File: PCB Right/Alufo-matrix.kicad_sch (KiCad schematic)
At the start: 62 parts, among them K11 PG1350, K12 PG1350, K13 PG1350, K14 PG1350, K15 PG1350, K16 PG1350, K21 PG1350, K22 PG1350, K23 PG1350, K24 PG1350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

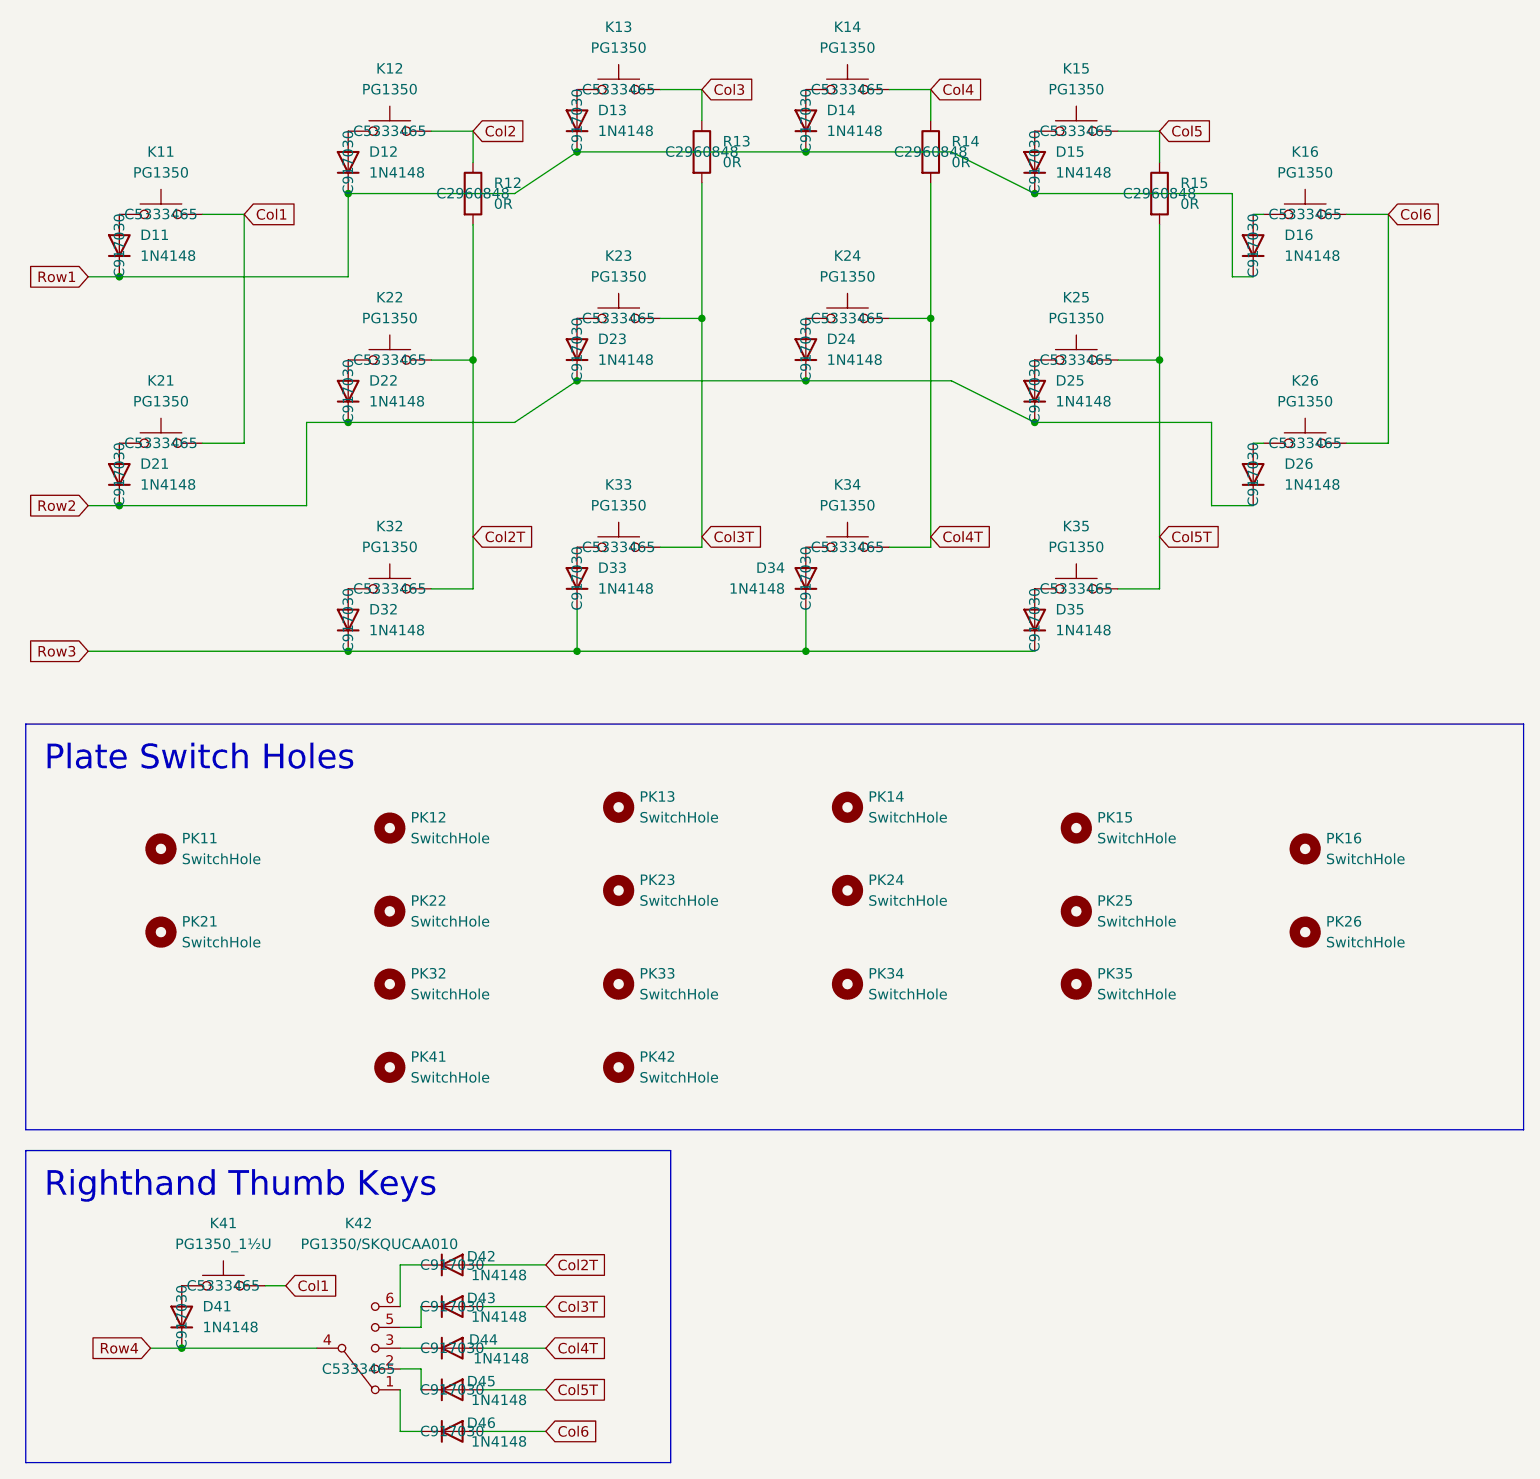
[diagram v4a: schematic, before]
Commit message: Update LCSC part number for USB ports
Also hide LCSC numbers erroneously showing in schematic.
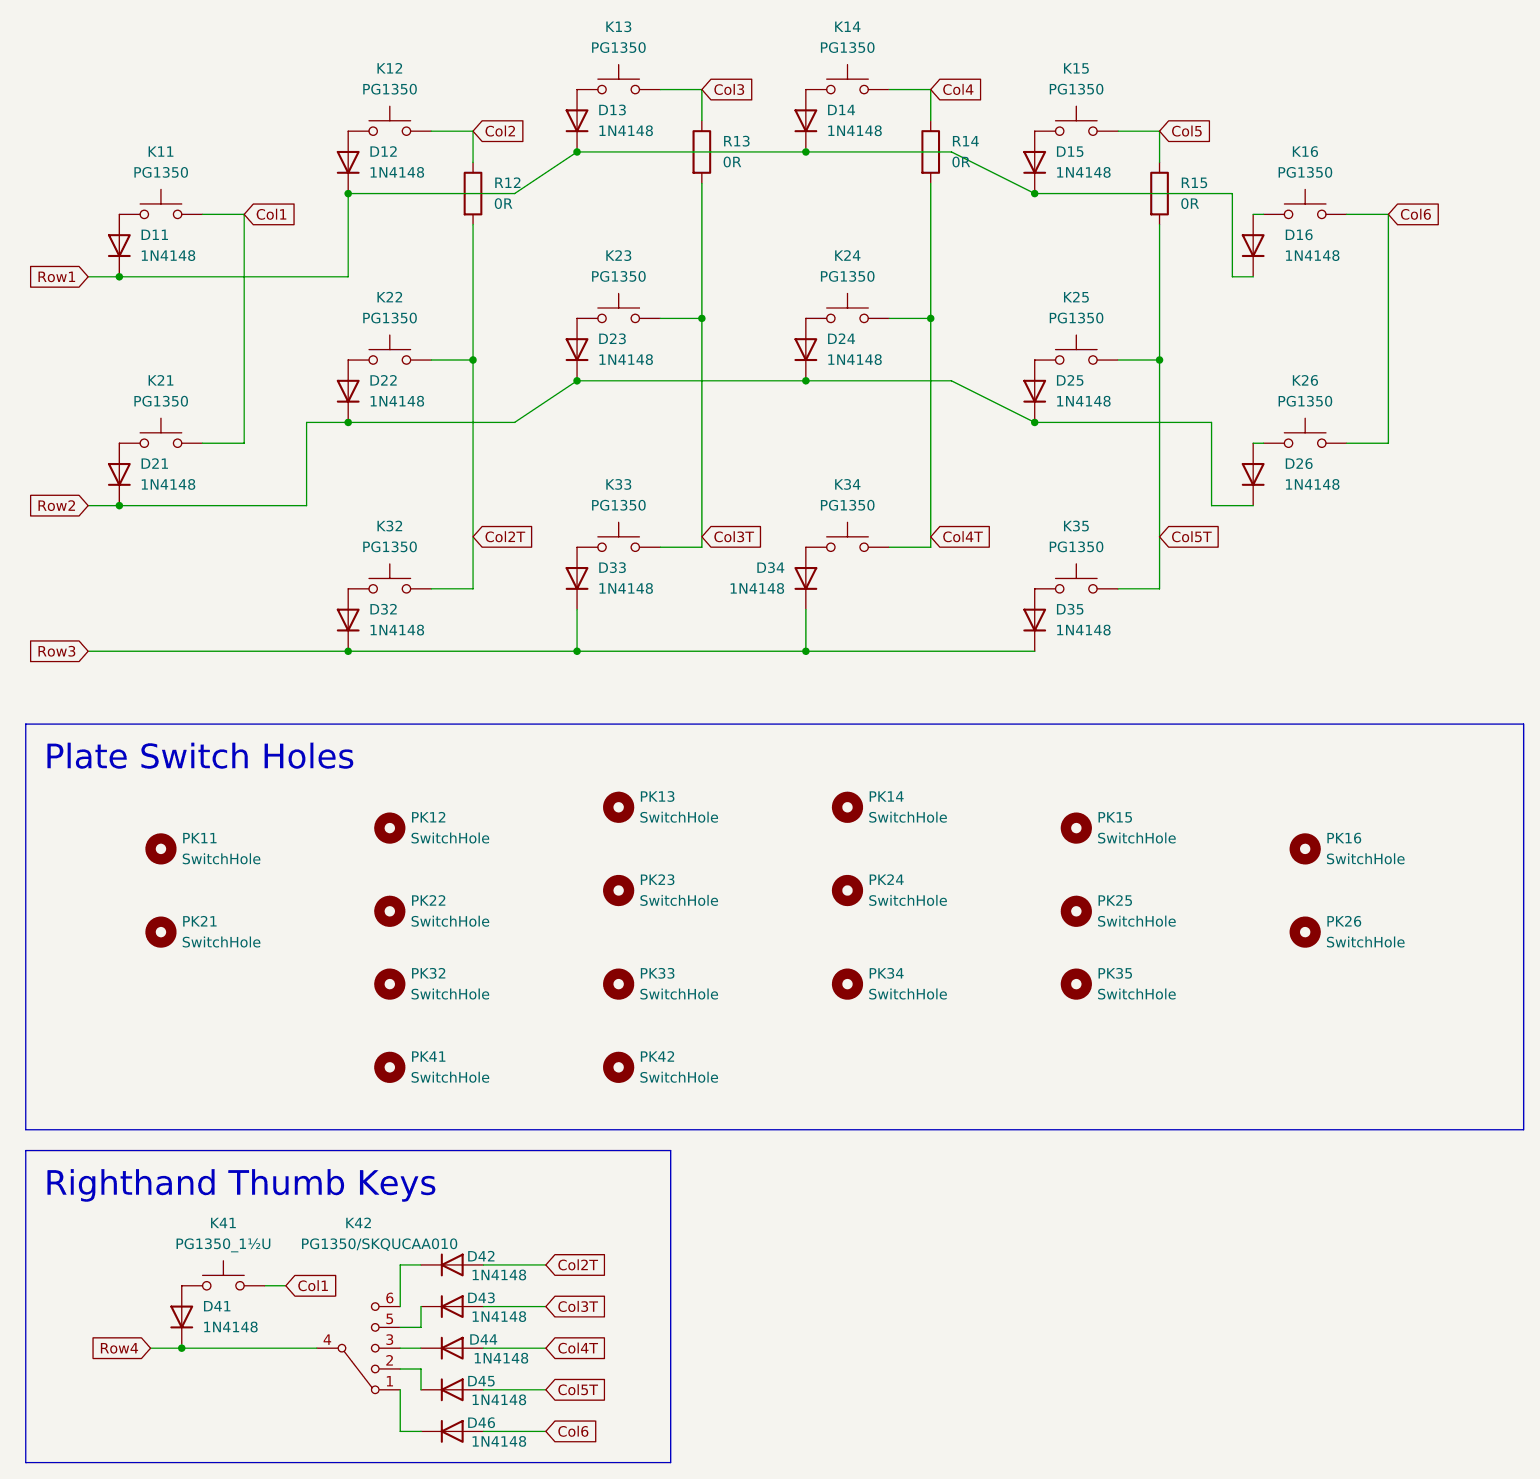
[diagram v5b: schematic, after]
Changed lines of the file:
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@@
 					(size 1.27 1.27)
 				)
+				(hide yes)
 			)
 		)
@@
 					(size 1.27 1.27)
 				)
+				(hide yes)
 			)
 		)
@@
 					(size 1.27 1.27)
 				)
+				(hide yes)
 			)
 		)
@@
 					(size 1.27 1.27)
 				)
+				(hide yes)
 			)
 		)
@@
 					(size 1.27 1.27)
 				)
+				(hide yes)
 			)
 		)
@@
 					(size 1.27 1.27)
 				)
+				(hide yes)
 			)
 		)
@@
 					(size 1.27 1.27)
 				)
+				(hide yes)
 			)
 		)
@@
 					(size 1.27 1.27)
 				)
+				(hide yes)
 			)
 		)
@@
 					(size 1.27 1.27)
 				)
+				(hide yes)
 			)
 		)
@@
 					(size 1.27 1.27)
 				)
+				(hide yes)
 			)
 		)
@@
 					(size 1.27 1.27)
 				)
+				(hide yes)
 			)
 		)
@@
 					(size 1.27 1.27)
 				)
+				(hide yes)
 			)
 		)
@@
 					(size 1.27 1.27)
 				)
+				(hide yes)
 			)
 		)
@@
 					(size 1.27 1.27)
 				)
+				(hide yes)
 			)
 		)
@@
 					(size 1.27 1.27)
 				)
+				(hide yes)
 			)
 		)
@@
 					(size 1.27 1.27)
 				)
+				(hide yes)
 			)
 		)
@@
 					(size 1.27 1.27)
 				)
+				(hide yes)
 			)
 		)
@@
 					(size 1.27 1.27)
 				)
+				(hide yes)
 			)
 		)
@@
 					(size 1.27 1.27)
 				)
+				(hide yes)
 			)
 		)
@@
 					(size 1.27 1.27)
 				)
+				(hide yes)
 			)
 		)
@@
 					(size 1.27 1.27)
 				)
+				(hide yes)
 			)
 		)
@@
 					(size 1.27 1.27)
 				)
+				(hide yes)
 			)
 		)
@@
 					(size 1.27 1.27)
 				)
+				(hide yes)
 			)
 		)
@@
 					(size 1.27 1.27)
 				)
+				(hide yes)
 			)
 		)
@@
 					(size 1.27 1.27)
 				)
+				(hide yes)
 			)
 		)
@@
 					(size 1.27 1.27)
 				)
+				(hide yes)
 			)
 		)
@@
 					(size 1.27 1.27)
 				)
+				(hide yes)
 			)
 		)
@@
 					(size 1.27 1.27)
 				)
+				(hide yes)
 			)
 		)
@@
 					(size 1.27 1.27)
 				)
+				(hide yes)
 			)
 		)
@@
 					(size 1.27 1.27)
 				)
+				(hide yes)
 			)
 		)
@@
 					(size 1.27 1.27)
 				)
+				(hide yes)
 			)
 		)
@@
 					(size 1.27 1.27)
 				)
+				(hide yes)
 			)
 		)
@@
 					(size 1.27 1.27)
 				)
+				(hide yes)
 			)
 		)
@@
 					(size 1.27 1.27)
 				)
+				(hide yes)
 			)
 		)
@@
 					(size 1.27 1.27)
 				)
+				(hide yes)
 			)
 		)
@@
 					(size 1.27 1.27)
 				)
+				(hide yes)
 			)
 		)
@@
 					(size 1.27 1.27)
 				)
+				(hide yes)
 			)
 		)
@@
 					(size 1.27 1.27)
 				)
+				(hide yes)
 			)
 		)
@@
 					(size 1.27 1.27)
 				)
+				(hide yes)
 			)
 		)
@@
 					(size 1.27 1.27)
 				)
+				(hide yes)
 			)
 		)
@@
 					(size 1.27 1.27)
 				)
+				(hide yes)
 			)
 		)
@@
 					(size 1.27 1.27)
 				)
+				(hide yes)
 			)
 		)
@@
 					(size 1.27 1.27)
 				)
+				(hide yes)
 			)
 		)
@@
 					(size 1.27 1.27)
 				)
+				(hide yes)
 			)
 		)
